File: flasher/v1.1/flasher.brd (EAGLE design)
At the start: 48 x 51 mm, 41 parts, among them IC1 ULN2004A_BIG_SMD, IC2 7805, Q1 IRF4905, Q2 IRF4905, Q3 MMBF170, Q4 MMBF170, Q5 MMBF170, Q6 MMBF170

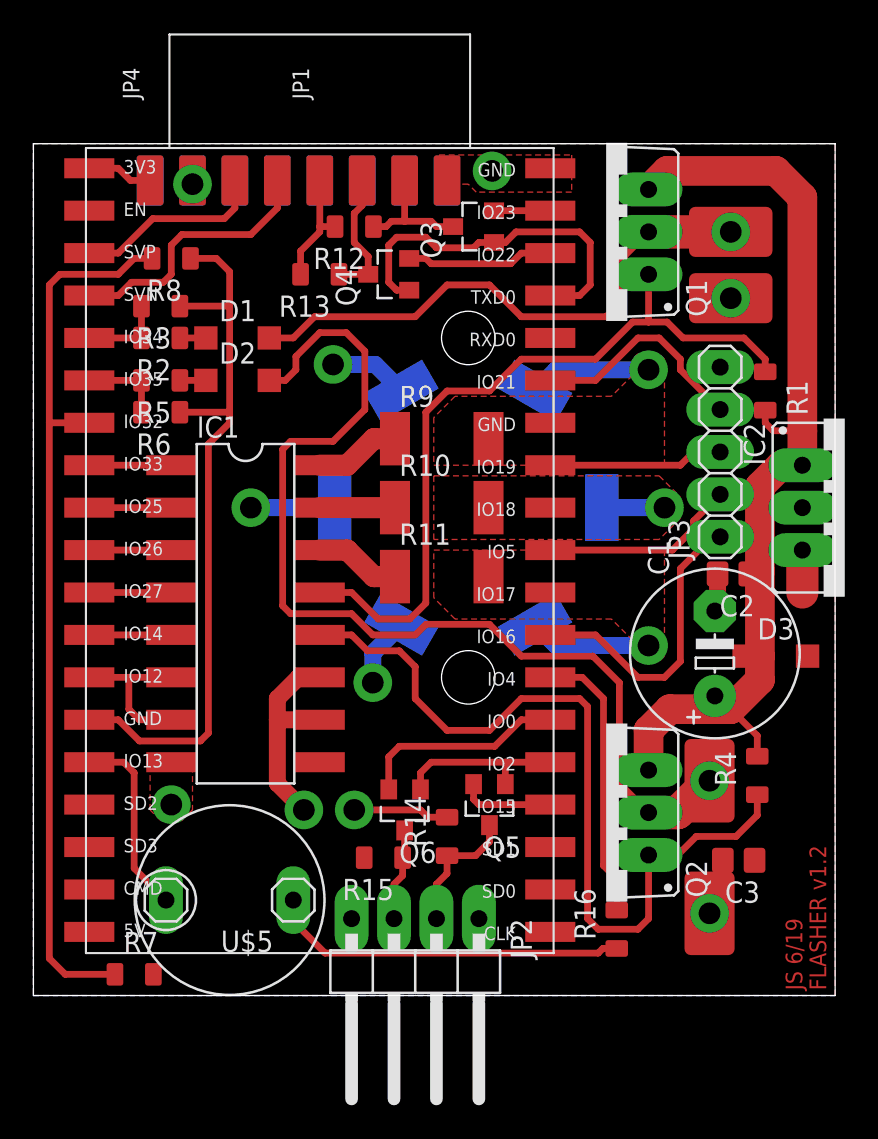
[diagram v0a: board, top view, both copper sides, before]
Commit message: Flasher v1.2: add reverse protection diode and capacitors to stabilizer, add some missing parts value, minor cosmetics changes
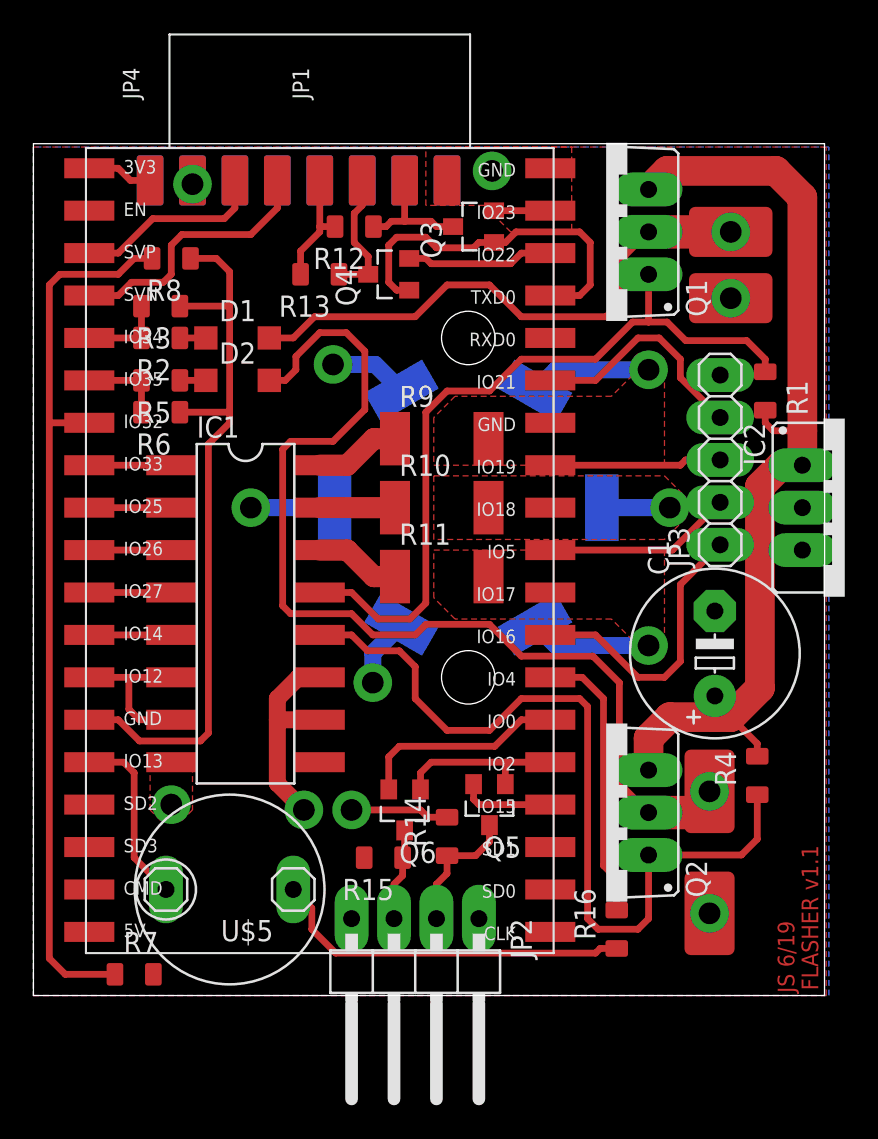
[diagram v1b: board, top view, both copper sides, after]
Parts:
- removed C2: 100n, rcl_upravena:C0805
- removed C3: 330n, rcl_upravena:C0805
- removed D3: (no value), diode:SOD123
- C1: value 330u/16V -> (none)
- IC2: value 7805 -> (none)
- Q3, Q4, Q5, Q6: value MMBF170 -> (none)
- moved U$3 0.63 mm to (40.5, 12.2)
- moved U$5 0.63 mm to (16.8, 5.08)
- moved JP3 0.48 mm to (41.1, 32.1)
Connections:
- net +5V: no longer C3.1, D3.A
- net GND: no longer C2.2, C3.2
- net VCC: no longer C2.1, D3.C
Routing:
- net GND: track 50.4 -> 44.6 mm
- net +5V: track 29.2 -> 26.9 mm
- net VCC: track 60.4 -> 58.8 mm
- net !PWR2_EN: track 49.9 -> 50.8 mm
- net IO16: track 18.0 -> 17.2 mm
- net BUZZ_P: track 11.4 -> 10.7 mm
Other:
- board size 48 x 51 mm -> 47.4 x 51 mm
- board text added: "FLASHER v1.1"
- board text removed: "FLASHER v1.2"
